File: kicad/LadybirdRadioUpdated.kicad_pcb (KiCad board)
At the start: 2 copper layers, 29 parts, among them J1 Conn_01x02_Pin, J2 Conn_01x02_Pin, J3 Conn_01x02_Pin, J4 Conn_01x03_Pin, Q1 BC547, Q2 BC337, Q3 BC337, T1 LT700

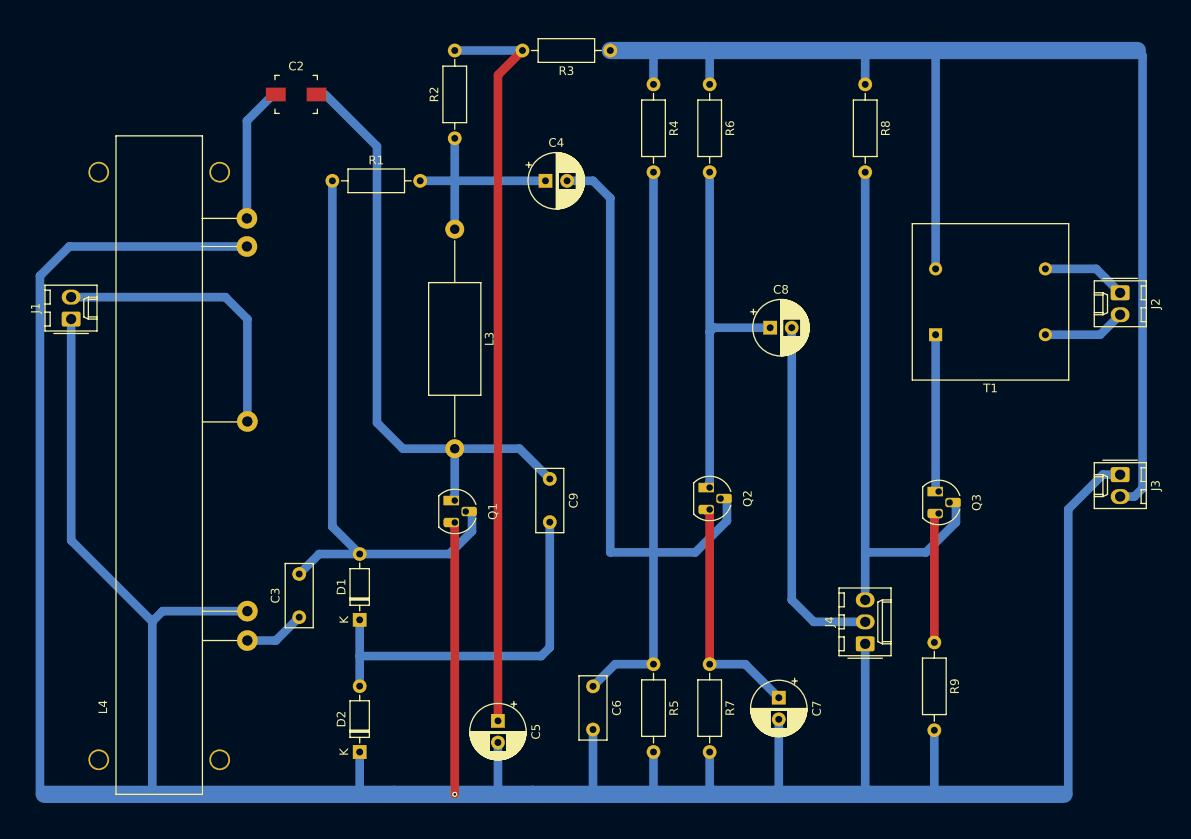
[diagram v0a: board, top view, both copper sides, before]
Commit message: Fixed transformer; Fixed temporary C-trimmer; Tidied ferrite; Tidied labels and values on silk screen
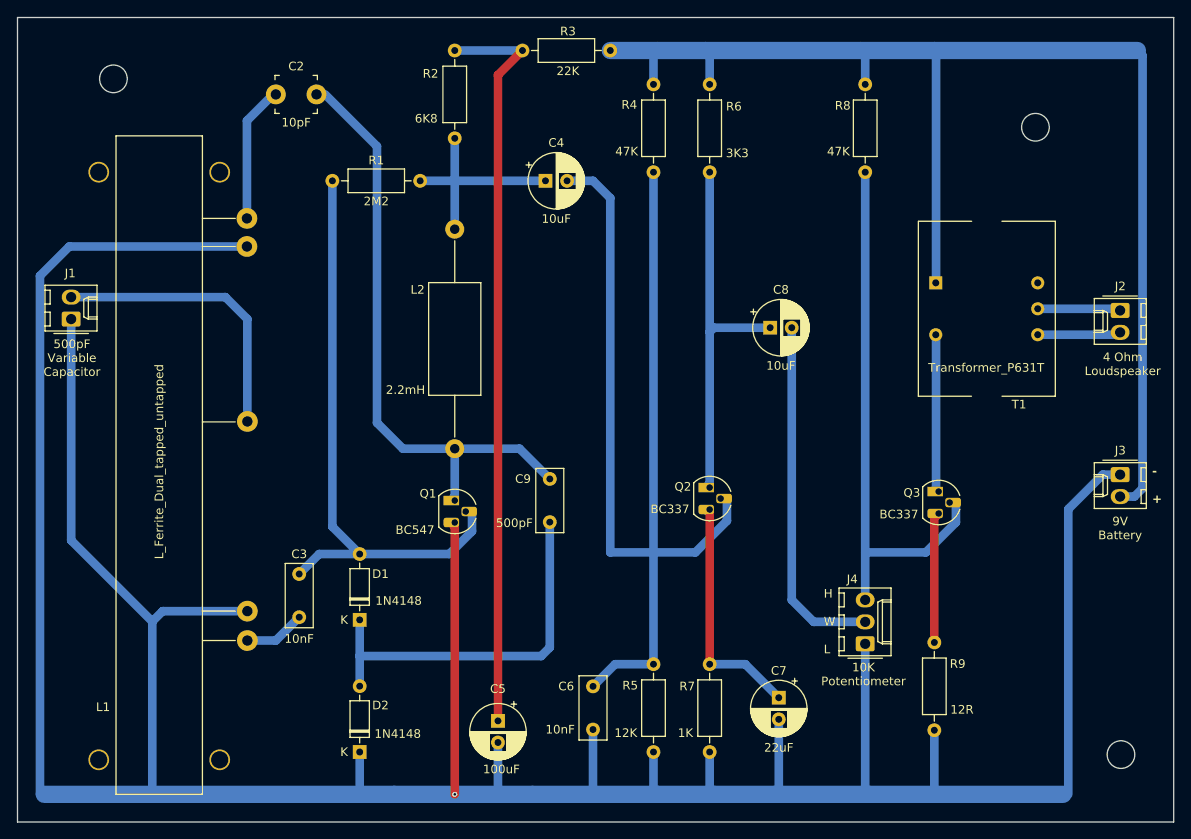
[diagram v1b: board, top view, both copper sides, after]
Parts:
- added REF**: MountingHole_3.2mm_M3, MountingHole:MountingHole_3.2mm_M3, F.Cu at (137.2, 46.8)
- added REF**: MountingHole_3.2mm_M3, MountingHole:MountingHole_3.2mm_M3, F.Cu at (30.5, 41.2)
- added REF**: MountingHole_3.2mm_M3, MountingHole:MountingHole_3.2mm_M3, F.Cu at (147.1, 119.4)
- C2: footprint Capacitor_SMD:C_Trimmer_Murata_TZB4-A -> ACRM:C_Trimmer_THT
- T1: value LT700 -> Transformer_P631T; footprint ACRM:Transformer_LT722 -> ACRM:Transformer_P631T
- moved T1 15.0 mm to (138.4, 63.0), turned to 0 degrees
- moved J2 2.04 mm to (147.0, 68.0)
- renumbered L4 to L1, L3 to L2
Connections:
- T1 pad 1: Net-(Q3-C) -> Net-(J3-Pin_2)
- T1 pad 2: Net-(J3-Pin_2) -> Net-(Q3-C)
- T1 pad 3: Net-(J2-Pin_1) -> Net-(J2-Pin_2)
- T1 pad 4: Net-(J2-Pin_2) -> Net-(J2-Pin_1)
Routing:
- net Net-(J3-Pin_2): track 152.6 -> 154.3 mm
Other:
- board outline added: 133.8 x 93.1 mm
- board text added: "- +"
- board text added: "10K Potentiometer"
- board text added: "4 Ohm Loudspeaker"
- board text added: "500pF Variable Capacitor"
- board text added: "9V Battery"
- board text added: "H W L"
